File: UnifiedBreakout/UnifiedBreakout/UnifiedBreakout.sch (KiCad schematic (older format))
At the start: 14 parts, among them J1 MESA P3, J10 LIM Z, J11 ENCODER OUT, J12 PENDANT, J13 DRAWBAR, J14 PROBE, J2 MESA P2, J3 ENCODER IN, J4 LIM X, J7 ATX-24, J9 LIM Y, K1 MOTOR POWER, K2 MIST, K3 DRAWBAR

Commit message: Unified breakout schematic "done"
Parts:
- removed J1: MESA P3, Connector_Dsub:DSUB-25_Female_Horizontal_P2.77x2.84mm_EdgePinOffset4.94mm_Housed_MountingHolesOffset7.48mm, symbol Connector:DB25_Female_MountingHoles
- removed J10: LIM Z, Connector_RJ:RJ12_Amphenol_54601, symbol Connector:RJ12
- removed J11: ENCODER OUT, Connector_Dsub:DSUB-15_Female_Horizontal_P2.77x2.84mm_EdgePinOffset4.94mm_Housed_MountingHolesOffset7.48mm, symbol Connector:DB15_Female_MountingHoles
- removed J12: PENDANT, Connector_Dsub:DSUB-25_Female_Horizontal_P2.77x2.84mm_EdgePinOffset4.94mm_Housed_MountingHolesOffset7.48mm, symbol Connector:DB25_Female_MountingHoles
- removed J13: DRAWBAR, Connector_RJ:RJ12_Amphenol_54601, symbol Connector:RJ12
- removed J14: PROBE, Connector_RJ:RJ12_Amphenol_54601, symbol Connector:RJ12
- removed J2: MESA P2, Connector_Dsub:DSUB-25_Female_Horizontal_P2.77x2.84mm_EdgePinOffset4.94mm_Housed_MountingHolesOffset7.48mm, symbol Connector:DB25_Female_MountingHoles
- removed J3: ENCODER IN, Connector_RJ:RJ45_Amphenol_54602-x08_Horizontal, symbol Connector:RJ45
- removed J4: LIM X, Connector_RJ:RJ12_Amphenol_54601, symbol Connector:RJ12
- removed J9: LIM Y, Connector_RJ:RJ12_Amphenol_54601, symbol Connector:RJ12
- removed K1: MOTOR POWER, Relay_THT:Relay_DPDT_Finder_40.52, symbol Relay:FINDER-40.52
- removed K2: MIST, Relay_THT:Relay_DPDT_Finder_40.52, symbol Relay:FINDER-40.52
- removed K3: DRAWBAR, Relay_THT:Relay_DPDT_Finder_40.52, symbol Relay:FINDER-40.52
- added C1, C3, C5, C7: 100n, Capacitor_THT:C_Rect_L7.0mm_W2.0mm_P5.00mm, symbol Device:C
- added C2, C4, C6, C8: 100uF, Capacitor_THT:CP_Radial_D6.3mm_P2.50mm, symbol Device:CP
- added D1: MESA P3 PWR, LED_THT:LED_D3.0mm, symbol Device:LED
- added D2: MESA P2 PWR, LED_THT:LED_D3.0mm, symbol Device:LED
- added D3: ATX PWR GOOD, LED_THT:LED_D3.0mm, symbol Device:LED
- added D4: ATX STBY, LED_THT:LED_D3.0mm, symbol Device:LED
- added J1: 24V DC, Connector_BarrelJack:BarrelJack_Horizontal, symbol Connector:Barrel_Jack_Switch
- added J3: 5V BUS, Connector_Phoenix_MSTB:PhoenixContact_MSTBA_2,5_2-G-5,08_1x02_P5.08mm_Horizontal, symbol Connector:Screw_Terminal_01x02
- added J4: 24V BUS, Connector_Phoenix_MSTB:PhoenixContact_MSTBA_2,5_2-G-5,08_1x02_P5.08mm_Horizontal, symbol Connector:Screw_Terminal_01x02
- added J5: 12V BUS, Connector_Phoenix_MSTB:PhoenixContact_MSTBA_2,5_2-G-5,08_1x02_P5.08mm_Horizontal, symbol Connector:Screw_Terminal_01x02
- added J6: ARGON RS485, Connector_Phoenix_MSTB:PhoenixContact_MSTBA_2,5_3-G-5,08_1x03_P5.08mm_Horizontal, symbol Connector:Screw_Terminal_01x03
- added R1, R7: 2K2, Resistor_THT:R_Axial_DIN0207_L6.3mm_D2.5mm_P10.16mm_Horizontal, symbol Device:R
- added R2, R3, R4, R5: 220R, Resistor_THT:R_Axial_DIN0207_L6.3mm_D2.5mm_P10.16mm_Horizontal, symbol Device:R
- added R6: 220K, Resistor_THT:R_Axial_DIN0207_L6.3mm_D2.5mm_P10.16mm_Horizontal, symbol Device:R
- added U1: 4N35, Package_DIP:DIP-6_W7.62mm, symbol Isolator:4N35
- renumbered J7 to J2
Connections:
- net labels added: +12V, +24V, +5V, +5VP, AXIS_PWR, DRAWBAR_SW, DRAWBAR_VALVE, ESTOP, GPI1, GPI2, LIMIT_X, LIMIT_Y, LIMIT_Z, MIST, PENDANT_ENC_A, PENDANT_ENC_B, PENDANT_MULX1, PENDANT_MULX10, PENDANT_MULX100, PENDANT_SELA, PENDANT_SELX, PENDANT_SELY, PENDANT_SELZ, PROBE, SPINDLE_ENC_A, SPINDLE_ENC_B, SPINDLE_ENC_IDX, SPINDLE_PWM_DIR, SPINDLE_PWM_SIG, SPINDLE_STEPGEN_DIR, SPINDLE_STEPGEN_STEP
- wire segments 6 -> 196
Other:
- moved on the sheet: J2

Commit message: Invert outputs for active low, other cleanup
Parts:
- added R24, R25, R26: 10K, Resistor_THT:R_Axial_DIN0207_L6.3mm_D2.5mm_P10.16mm_Horizontal, symbol Device:R
- added U7: 74HC14, Package_DIP:DIP-14_W7.62mm_LongPads, symbol 74xx:74HC14
- J2: footprint Connector_Molex:Molex_Mini-Fit_Jr_5566-24A_2x12_P4.20mm_Vertical -> Connector_Molex:Molex_Mini-Fit_Jr_5569-24A2_2x12_P4.20mm_Horizontal
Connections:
- net +5VP: now also R24.1, R25.1, R26.1
- net AXIS_PWR: now also R24.2, U7.1
- net DRAWBAR_VALVE: now also R25.2, U7.3
- net MIST: now also R26.2, U7.5
- net ATX_PWR: now reaches J2.16 (PS_ON#), R1.2
- new net AXIS POWER RELAY/ENABLE: U7.2
- new net DRAWBAR RELAY/ENABLE: U7.4
- new net MIST RELAY/ENABLE: U7.6
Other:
- moved on the sheet: C1, C2, C3, C4, C5, C6, C7, C8, D3, D4, J1, J2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

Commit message: Add extra pullups on inputs
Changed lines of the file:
@@
 F4 "24V" U R 11850 1200 50
 F5 "5V" U R 11850 1350 50
+F6 "MESA_5V" U L 10950 1500 50
 $EndSheet
 $Comp
@@
 F4 "24V" U R 11850 2200 50
 F5 "5V" U R 11850 2350 50
+F6 "MESA_5V" U L 10950 2500 50
 $EndSheet
 $Comp
@@
 F4 "24V" U R 11850 3200 50
 F5 "5V" U R 11850 3350 50
+F6 "MESA_5V" U L 10950 3500 50
 $EndSheet
 $Comp
@@
 F4 "24V" U R 11850 4200 50
 F5 "5V" U R 11850 4350 50
+F6 "MESA_5V" U L 10950 4500 50
 $EndSheet
 $Comp
@@
 F4 "24V" U R 11850 5200 50
 F5 "5V" U R 11850 5350 50
+F6 "MESA_5V" U L 10950 5500 50
 $EndSheet
 $Comp
@@
 Text Label 5250 3550 2    50   ~ 0
 ALARM
+$Comp
+L power:+5VP #PWR0104
+U 1 1 5E9E7D4E
+P 10650 5500
+F 0 "#PWR0104" H 10650 5350 50  0001 C CNN
+F 1 "+5VP" H 10665 5673 50  0000 C CNN
+F 2 "" H 10650 5500 50  0001 C CNN
+F 3 "" H 10650 5500 50  0001 C CNN
+	1    10650 5500
+	1    0    0    -1
+$EndComp
+Wire Wire Line
+	10950 5500 10650 5500
+$Comp
+L power:+5VP #PWR0105
+U 1 1 5E9F5A09
+P 10650 4500
+F 0 "#PWR0105" H 10650 4350 50  0001 C CNN
+F 1 "+5VP" H 10665 4673 50  0000 C CNN
+F 2 "" H 10650 4500 50  0001 C CNN
+F 3 "" H 10650 4500 50  0001 C CNN
+	1    10650 4500
+	1    0    0    -1
+$EndComp
+Wire Wire Line
+	10950 4500 10650 4500
+$Comp
+L power:+5VP #PWR0106
+U 1 1 5EA027BB
+P 10650 3500
+F 0 "#PWR0106" H 10650 3350 50  0001 C CNN
+F 1 "+5VP" H 10665 3673 50  0000 C CNN
+F 2 "" H 10650 3500 50  0001 C CNN
+F 3 "" H 10650 3500 50  0001 C CNN
+	1    10650 3500
+	1    0    0    -1
+$EndComp
+Wire Wire Line
+	10950 3500 10650 3500
+$Comp
+L power:+5VP #PWR0107
+U 1 1 5EA0F70E
+P 10650 2500
+F 0 "#PWR0107" H 10650 2350 50  0001 C CNN
+F 1 "+5VP" H 10665 2673 50  0000 C CNN
+F 2 "" H 10650 2500 50  0001 C CNN
+F 3 "" H 10650 2500 50  0001 C CNN
+	1    10650 2500
+	1    0    0    -1
+$EndComp
+Wire Wire Line
+	10950 2500 10650 2500
+$Comp
+L power:+5VP #PWR0108
+U 1 1 5EA1CA67
+P 10650 1500
+F 0 "#PWR0108" H 10650 1350 50  0001 C CNN
+F 1 "+5VP" H 10665 1673 50  0000 C CNN
+F 2 "" H 10650 1500 50  0001 C CNN
+F 3 "" H 10650 1500 50  0001 C CNN
+	1    10650 1500
+	1    0    0    -1
+$EndComp
+Wire Wire Line
+	10950 1500 10650 1500
 $EndSCHEMATC

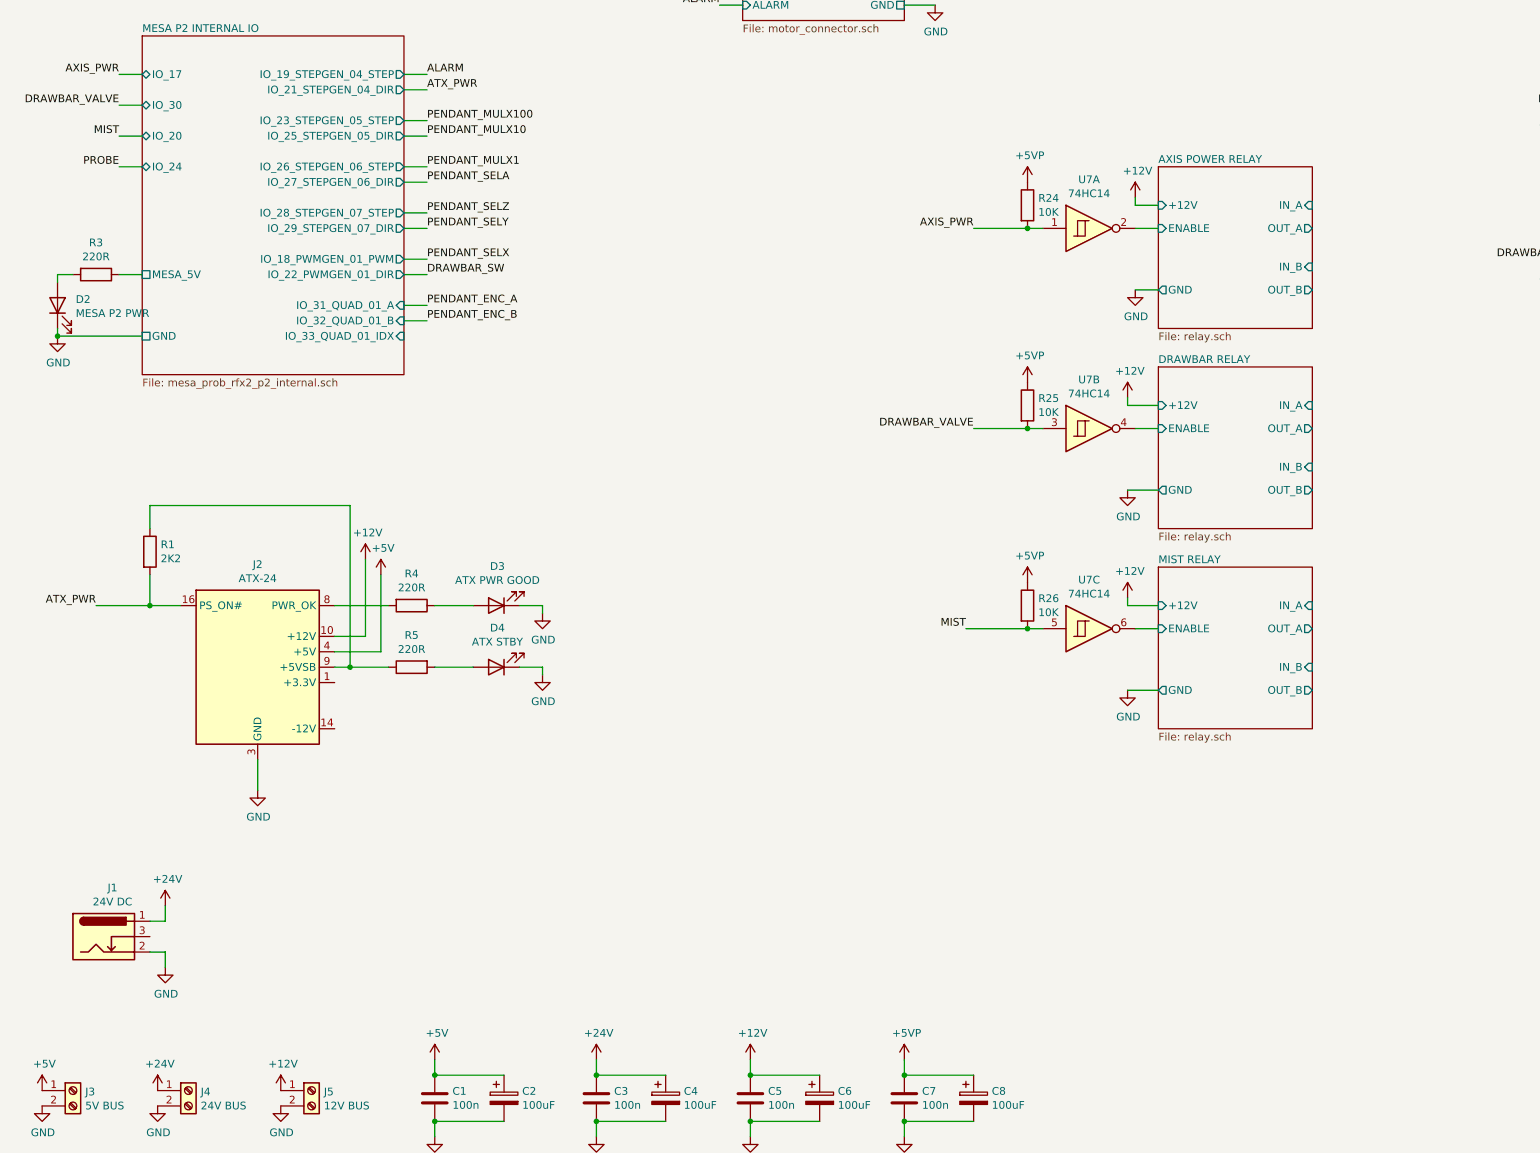
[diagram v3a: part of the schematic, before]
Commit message: Connectors placed
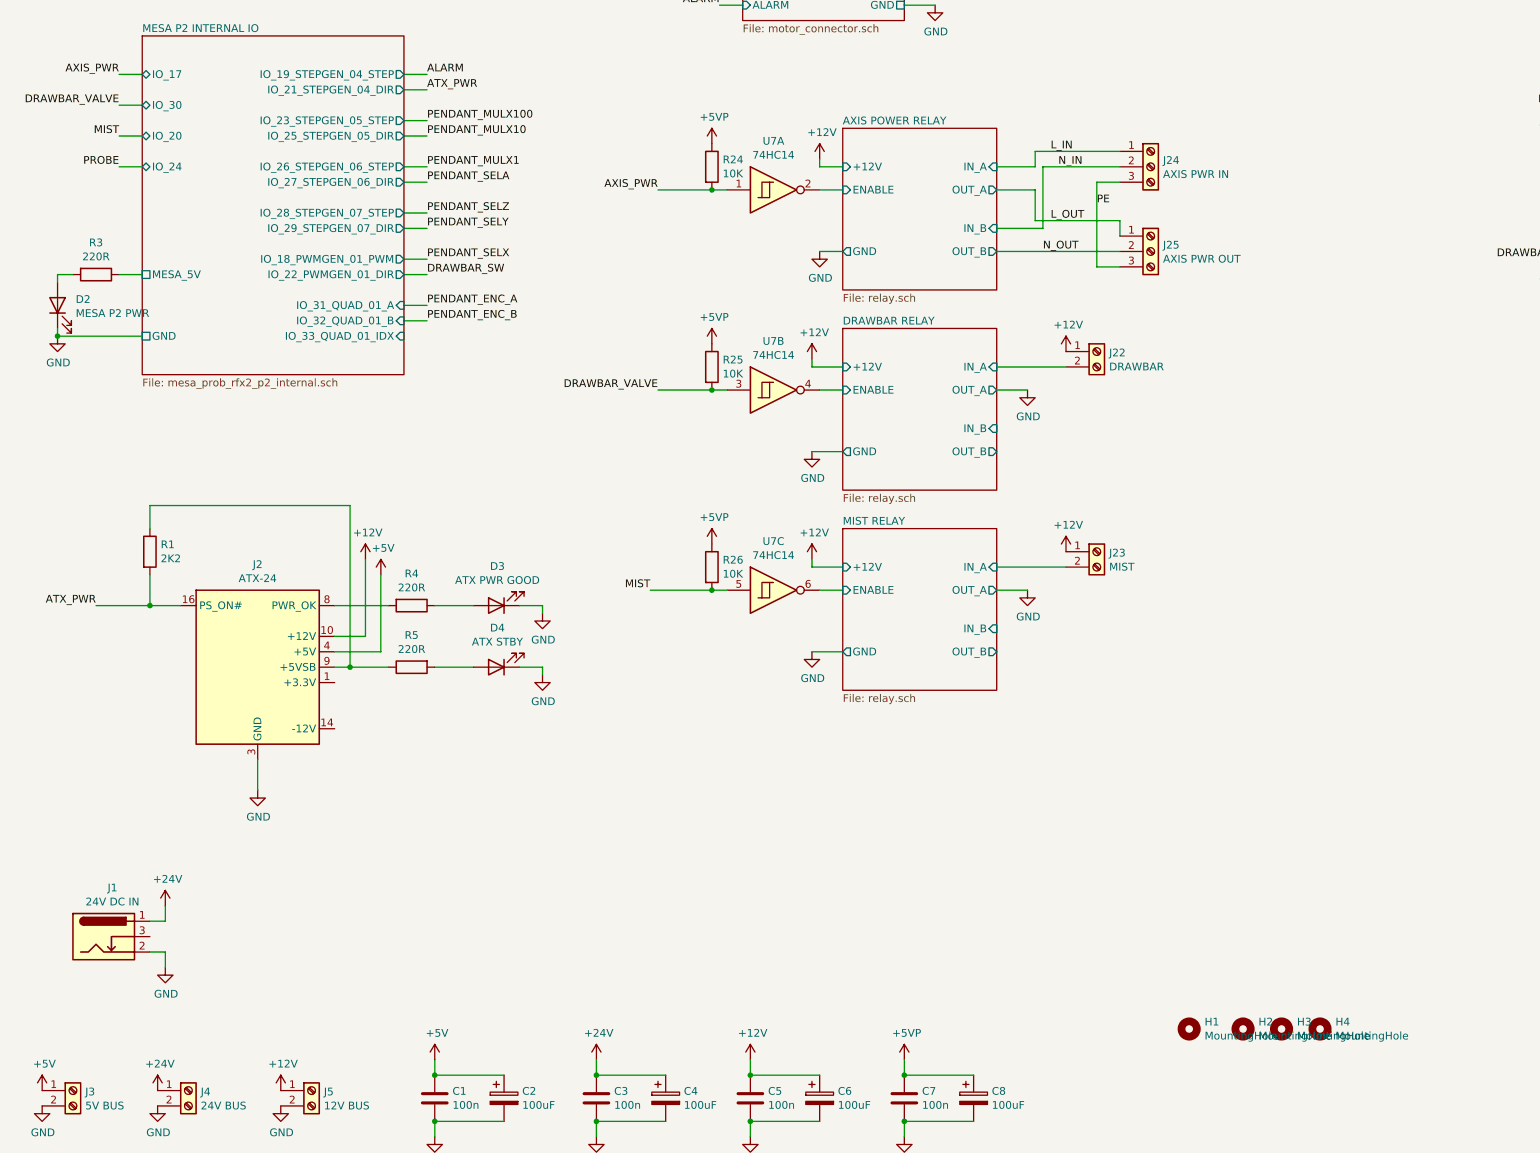
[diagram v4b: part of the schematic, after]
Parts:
- added H1, H2, H3, H4: MountingHole, MountingHole:MountingHole_3.2mm_M3, symbol Mechanical:MountingHole
- added J22: DRAWBAR, Connector_Phoenix_MSTB:PhoenixContact_MSTBA_2,5_2-G-5,08_1x02_P5.08mm_Horizontal, symbol Connector:Screw_Terminal_01x02
- added J23: MIST, Connector_Phoenix_MSTB:PhoenixContact_MSTBA_2,5_2-G-5,08_1x02_P5.08mm_Horizontal, symbol Connector:Screw_Terminal_01x02
- added J24: AXIS PWR IN, Connector_Phoenix_MSTB:PhoenixContact_MSTBA_2,5_3-G-5,08_1x03_P5.08mm_Horizontal, symbol Connector:Screw_Terminal_01x03
- added J25: AXIS PWR OUT, Connector_Phoenix_MSTB:PhoenixContact_MSTBA_2,5_3-G-5,08_1x03_P5.08mm_Horizontal, symbol Connector:Screw_Terminal_01x03
- J1: value 24V DC -> 24V DC IN
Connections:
- net +12V: now also J22.1 (Pin_1), J23.1 (Pin_1)
- net DRAWBAR RELAY/IN_A: now also J22.2 (Pin_2)
- net MIST RELAY/IN_A: now also J23.2 (Pin_2)
- new net L_IN: J24.1 (Pin_1)
- new net L_OUT: J25.1 (Pin_1)
- new net N_IN: J24.2 (Pin_2)
- new net N_OUT: J25.2 (Pin_2)
- new net PE: J24.3 (Pin_3), J25.3 (Pin_3)
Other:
- moved on the sheet: R24, R25, R26, U7A, U7B, U7C

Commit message: More placement, add some custom parts
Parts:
- J1: footprint Connector_BarrelJack:BarrelJack_Horizontal -> SwitchCraft-BarrelJack-RAPC722BK:RAPC722BK
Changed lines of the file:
@@
 F 0 "J1" H 1307 9917 50  0000 C CNN
 F 1 "24V DC IN" H 1307 9826 50  0000 C CNN
-F 2 "Connector_BarrelJack:BarrelJack_Horizontal" H 1300 9560 50  0001 C CNN
+F 2 "SwitchCraft-BarrelJack-RAPC722BK:RAPC722BK" H 1300 9560 50  0001 C CNN
 F 3 "~" H 1300 9560 50  0001 C CNN
 	1    1250 9600

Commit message: Assigned some parts
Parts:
- C1, C3, C5, C7: footprint Capacitor_THT:C_Rect_L7.0mm_W2.0mm_P5.00mm -> Capacitor_THT:C_Disc_D5.0mm_W2.5mm_P2.50mm; MPN (none) -> K104K15X7RF53H5; Manufacturer (none) -> Vishay
- C2, C4, C6, C8: footprint Capacitor_THT:CP_Radial_D6.3mm_P2.50mm -> Capacitor_THT:CP_Radial_D8.0mm_P3.50mm; MPN (none) -> 515D107M035BB6AE3; Manufacturer (none) -> Vishay
- J1: MPN (none) -> RAPC722BK; Manufacturer (none) -> Switchcraft
- R1, R7: MPN (none) -> CFR-25JB-52-2K2; Manufacturer (none) -> Yageo
- R2, R3, R4, R5: MPN (none) -> CFR-25JB-52-220R; Manufacturer (none) -> Yageo
- R24, R25, R26: MPN (none) -> CFR-25JB-52-10K; Manufacturer (none) -> Yageo
- R6: MPN (none) -> CFR-25JB-52-220K; Manufacturer (none) -> Yageo
- U1: MPN (none) -> 4N35; Manufacturer (none) -> Vishay
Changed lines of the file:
@@
 F 0 "C3" H 4565 10696 50  0000 L CNN
 F 1 "100n" H 4565 10605 50  0000 L CNN
-F 2 "Capacitor_THT:C_Rect_L7.0mm_W2.0mm_P5.00mm" H 4488 10500 50  0001 C CNN
+F 2 "Capacitor_THT:C_Disc_D5.0mm_W2.5mm_P2.50mm" H 4488 10500 50  0001 C CNN
 F 3 "~" H 4450 10650 50  0001 C CNN
+F 4 "K104K15X7RF53H5" H 4450 10650 50  0001 C CNN "MPN"
+F 5 "Vishay" H 4450 10650 50  0001 C CNN "Manufacturer"
 	1    4450 10650
 	1    0    0    -1
@@
 F 0 "C4" H 5018 10696 50  0000 L CNN
 F 1 "100uF" H 5018 10605 50  0000 L CNN
-F 2 "Capacitor_THT:CP_Radial_D6.3mm_P2.50mm" H 4938 10500 50  0001 C CNN
+F 2 "Capacitor_THT:CP_Radial_D8.0mm_P3.50mm" H 4938 10500 50  0001 C CNN
 F 3 "~" H 4900 10650 50  0001 C CNN
+F 4 "515D107M035BB6AE3" H 4900 10650 50  0001 C CNN "MPN"
+F 5 "Vishay" H 4900 10650 50  0001 C CNN "Manufacturer"
 	1    4900 10650
 	1    0    0    -1
@@
 F 0 "C1" H 3515 10696 50  0000 L CNN
 F 1 "100n" H 3515 10605 50  0000 L CNN
-F 2 "Capacitor_THT:C_Rect_L7.0mm_W2.0mm_P5.00mm" H 3438 10500 50  0001 C CNN
+F 2 "Capacitor_THT:C_Disc_D5.0mm_W2.5mm_P2.50mm" H 3438 10500 50  0001 C CNN
 F 3 "~" H 3400 10650 50  0001 C CNN
+F 4 "K104K15X7RF53H5" H 3400 10650 50  0001 C CNN "MPN"
+F 5 "Vishay" H 3400 10650 50  0001 C CNN "Manufacturer"
 	1    3400 10650
 	1    0    0    -1
@@
 F 0 "C2" H 3968 10696 50  0000 L CNN
 F 1 "100uF" H 3968 10605 50  0000 L CNN
-F 2 "Capacitor_THT:CP_Radial_D6.3mm_P2.50mm" H 3888 10500 50  0001 C CNN
+F 2 "Capacitor_THT:CP_Radial_D8.0mm_P3.50mm" H 3888 10500 50  0001 C CNN
 F 3 "~" H 3850 10650 50  0001 C CNN
+F 4 "515D107M035BB6AE3" H 3850 10650 50  0001 C CNN "MPN"
+F 5 "Vishay" H 3850 10650 50  0001 C CNN "Manufacturer"
 	1    3850 10650
 	1    0    0    -1
@@
 F 0 "C5" H 5565 10696 50  0000 L CNN
 F 1 "100n" H 5565 10605 50  0000 L CNN
-F 2 "Capacitor_THT:C_Rect_L7.0mm_W2.0mm_P5.00mm" H 5488 10500 50  0001 C CNN
+F 2 "Capacitor_THT:C_Disc_D5.0mm_W2.5mm_P2.50mm" H 5488 10500 50  0001 C CNN
 F 3 "~" H 5450 10650 50  0001 C CNN
+F 4 "K104K15X7RF53H5" H 5450 10650 50  0001 C CNN "MPN"
+F 5 "Vishay" H 5450 10650 50  0001 C CNN "Manufacturer"
 	1    5450 10650
 	1    0    0    -1
@@
 F 0 "C6" H 6018 10696 50  0000 L CNN
 F 1 "100uF" H 6018 10605 50  0000 L CNN
-F 2 "Capacitor_THT:CP_Radial_D6.3mm_P2.50mm" H 5938 10500 50  0001 C CNN
+F 2 "Capacitor_THT:CP_Radial_D8.0mm_P3.50mm" H 5938 10500 50  0001 C CNN
 F 3 "~" H 5900 10650 50  0001 C CNN
+F 4 "515D107M035BB6AE3" H 5900 10650 50  0001 C CNN "MPN"
+F 5 "Vishay" H 5900 10650 50  0001 C CNN "Manufacturer"
 	1    5900 10650
 	1    0    0    -1
@@
 F 2 "Resistor_THT:R_Axial_DIN0207_L6.3mm_D2.5mm_P10.16mm_Horizontal" V 3180 7450 50  0001 C CNN
 F 3 "~" H 3250 7450 50  0001 C CNN
+F 4 "CFR-25JB-52-220R" H 3250 7450 50  0001 C CNN "MPN"
+F 5 "Yageo" H 3250 7450 50  0001 C CNN "Manufacturer"
 	1    3250 7450
 	0    1    1    0
@@
 F 2 "Resistor_THT:R_Axial_DIN0207_L6.3mm_D2.5mm_P10.16mm_Horizontal" V 1480 7100 50  0001 C CNN
 F 3 "~" H 1550 7100 50  0001 C CNN
+F 4 "CFR-25JB-52-2K2" H 1550 7100 50  0001 C CNN "MPN"
+F 5 "Yageo" H 1550 7100 50  0001 C CNN "Manufacturer"
 	1    1550 7100
 	1    0    0    -1
@@
 F 2 "Resistor_THT:R_Axial_DIN0207_L6.3mm_D2.5mm_P10.16mm_Horizontal" V 3180 7850 50  0001 C CNN
 F 3 "~" H 3250 7850 50  0001 C CNN
+F 4 "CFR-25JB-52-220R" H 3250 7850 50  0001 C CNN "MPN"
+F 5 "Yageo" H 3250 7850 50  0001 C CNN "Manufacturer"
 	1    3250 7850
 	0    -1   1    0
@@
 F 0 "C7" H 6565 10696 50  0000 L CNN
 F 1 "100n" H 6565 10605 50  0000 L CNN
-F 2 "Capacitor_THT:C_Rect_L7.0mm_W2.0mm_P5.00mm" H 6488 10500 50  0001 C CNN
+F 2 "Capacitor_THT:C_Disc_D5.0mm_W2.5mm_P2.50mm" H 6488 10500 50  0001 C CNN
 F 3 "~" H 6450 10650 50  0001 C CNN
+F 4 "K104K15X7RF53H5" H 6450 10650 50  0001 C CNN "MPN"
+F 5 "Vishay" H 6450 10650 50  0001 C CNN "Manufacturer"
 	1    6450 10650
 	1    0    0    -1
@@
 F 0 "C8" H 7018 10696 50  0000 L CNN
 F 1 "100uF" H 7018 10605 50  0000 L CNN
-F 2 "Capacitor_THT:CP_Radial_D6.3mm_P2.50mm" H 6938 10500 50  0001 C CNN
+F 2 "Capacitor_THT:CP_Radial_D8.0mm_P3.50mm" H 6938 10500 50  0001 C CNN
 F 3 "~" H 6900 10650 50  0001 C CNN
+F 4 "515D107M035BB6AE3" H 6900 10650 50  0001 C CNN "MPN"
+F 5 "Vishay" H 6900 10650 50  0001 C CNN "Manufacturer"
 	1    6900 10650
 	1    0    0    -1
@@
 F 2 "Resistor_THT:R_Axial_DIN0207_L6.3mm_D2.5mm_P10.16mm_Horizontal" V 980 2500 50  0001 C CNN
 F 3 "~" H 1050 2500 50  0001 C CNN
+F 4 "CFR-25JB-52-220R" H 1050 2500 50  0001 C CNN "MPN"
+F 5 "Yageo" H 1050 2500 50  0001 C CNN "Manufacturer"
 	1    1050 2500
 	0    -1   -1   0
@@
 F 2 "Resistor_THT:R_Axial_DIN0207_L6.3mm_D2.5mm_P10.16mm_Horizontal" V 1130 5300 50  0001 C CNN
 F 3 "~" H 1200 5300 50  0001 C CNN
+F 4 "CFR-25JB-52-220R" H 1200 5300 50  0001 C CNN "MPN"
+F 5 "Yageo" H 1200 5300 50  0001 C CNN "Manufacturer"
 	1    1200 5300
 	0    1    1    0
@@
 F 2 "SwitchCraft-BarrelJack-RAPC722BK:RAPC722BK" H 1300 9560 50  0001 C CNN
 F 3 "~" H 1300 9560 50  0001 C CNN
+F 4 "RAPC722BK" H 1250 9600 50  0001 C CNN "MPN"
+F 5 "Switchcraft" H 1250 9600 50  0001 C CNN "Manufacturer"
 	1    1250 9600
 	1    0    0    -1
@@
 F 2 "Package_DIP:DIP-6_W7.62mm" H 12200 7800 50  0001 L CIN
 F 3 "https://www.vishay.com/docs/81181/4n35.pdf" H 12400 8000 50  0001 L CNN
+F 4 "4N35" H 12400 8000 50  0001 C CNN "MPN"
+F 5 "Vishay" H 12400 8000 50  0001 C CNN "Manufacturer"
 	1    12400 8000
 	-1   0    0    -1
@@
 F 2 "Resistor_THT:R_Axial_DIN0207_L6.3mm_D2.5mm_P10.16mm_Horizontal" V 11680 8350 50  0001 C CNN
 F 3 "~" H 11750 8350 50  0001 C CNN
+F 4 "CFR-25JB-52-220K" H 11750 8350 50  0001 C CNN "MPN"
+F 5 "Yageo" H 11750 8350 50  0001 C CNN "Manufacturer"
 	1    11750 8350
 	1    0    0    -1
@@
 F 2 "Resistor_THT:R_Axial_DIN0207_L6.3mm_D2.5mm_P10.16mm_Horizontal" V 12830 8100 50  0001 C CNN
 F 3 "~" H 12900 8100 50  0001 C CNN
+F 4 "CFR-25JB-52-2K2" H 12900 8100 50  0001 C CNN "MPN"
+F 5 "Yageo" H 12900 8100 50  0001 C CNN "Manufacturer"
 	1    12900 8100
 	0    -1   1    0
@@
 F 2 "Resistor_THT:R_Axial_DIN0207_L6.3mm_D2.5mm_P10.16mm_Horizontal" V 5130 4600 50  0001 C CNN
 F 3 "~" H 5200 4600 50  0001 C CNN
+F 4 "CFR-25JB-52-10K " H 5200 4600 50  0001 C CNN "MPN"
+F 5 "Yageo" H 5200 4600 50  0001 C CNN "Manufacturer"
 	1    5200 4600
 	1    0    0    -1
@@
 F 2 "Resistor_THT:R_Axial_DIN0207_L6.3mm_D2.5mm_P10.16mm_Horizontal" V 5130 5900 50  0001 C CNN
 F 3 "~" H 5200 5900 50  0001 C CNN
+F 4 "CFR-25JB-52-10K " H 5200 5900 50  0001 C CNN "MPN"
+F 5 "Yageo" H 5200 5900 50  0001 C CNN "Manufacturer"
 	1    5200 5900
 	1    0    0    -1
@@
 F 2 "Resistor_THT:R_Axial_DIN0207_L6.3mm_D2.5mm_P10.16mm_Horizontal" V 5130 7200 50  0001 C CNN
 F 3 "~" H 5200 7200 50  0001 C CNN
+F 4 "CFR-25JB-52-10K " H 5200 7200 50  0001 C CNN "MPN"
+F 5 "Yageo" H 5200 7200 50  0001 C CNN "Manufacturer"
 	1    5200 7200
 	1    0    0    -1
